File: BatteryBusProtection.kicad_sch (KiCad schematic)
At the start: 14 parts, among them Q10 SIRA99DP-T1-GE3, Q7 SIRA99DP-T1-GE3, Q8 SIRA99DP-T1-GE3, Q9 SIRA99DP-T1-GE3, U3 LTC4412xS6, U4 LTC4412xS6

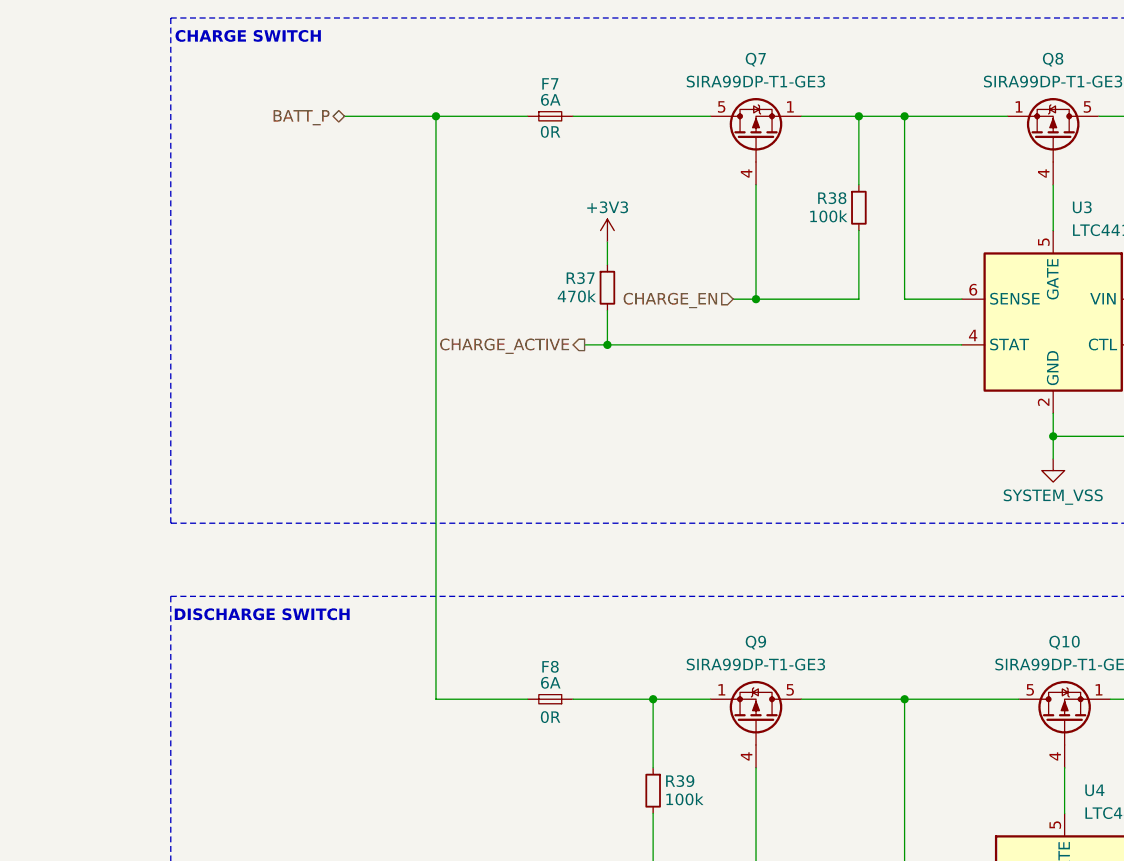
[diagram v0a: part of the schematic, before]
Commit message: Replaced old Interfaces with MCU
Added STM32U375CET6 mcu to board controlling the heaters and charging based on fuel gauge output.

Uses CAN for communication with mainboard.
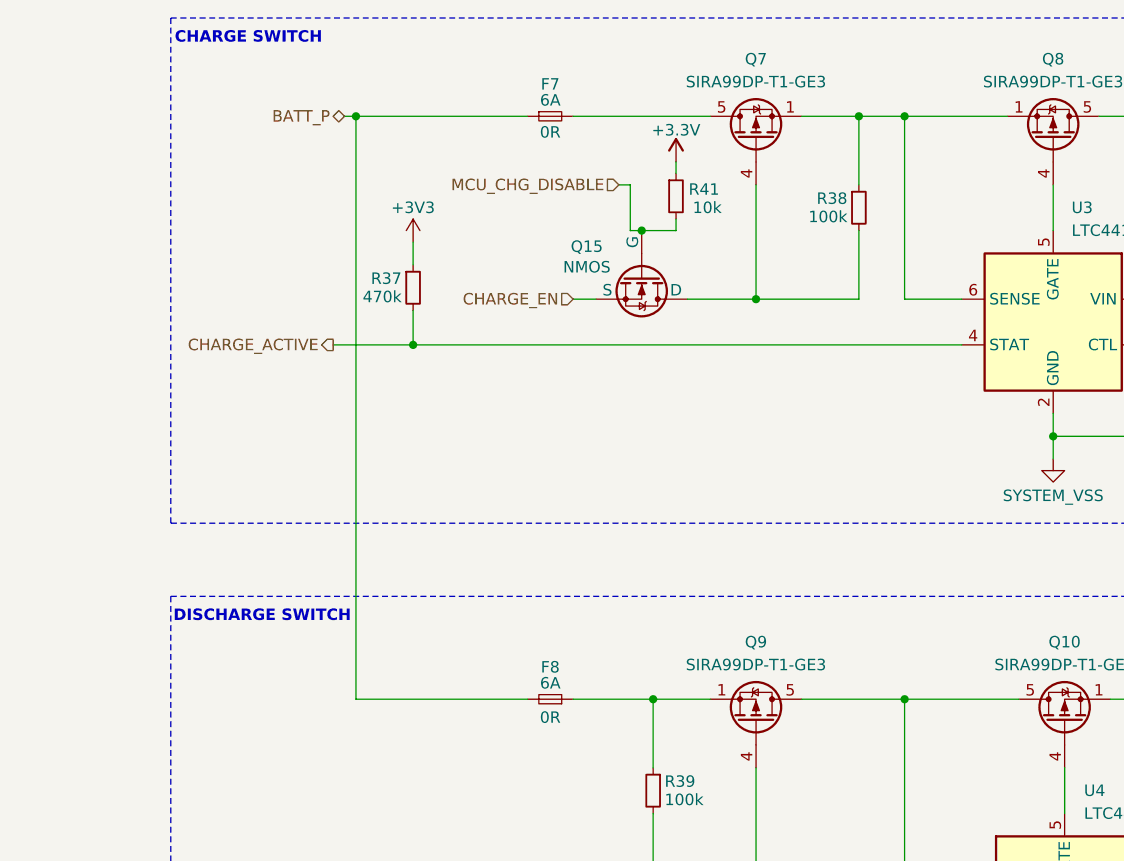
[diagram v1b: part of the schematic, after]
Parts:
- added Q15: NMOS, symbol Simulation_SPICE:NMOS
- added R41: 10k, Resistor_SMD:R_0603_1608Metric, symbol Device:R_Small
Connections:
- net CHARGE_EN: now also Q15.3 (S); no longer Q7.4 (G), R38.2
- new net: Q15.1 (D), Q7.4 (G), R38.2
- new net +3.3V: R41.1
- new net MCU_CHG_DISABLE: Q15.2 (G), R41.2
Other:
- moved on the sheet: R37

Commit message: Layout in progress
In the middle of completing layout
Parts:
- Q15: value NMOS -> IRLML2803; footprint (none) -> Package_TO_SOT_SMD:SOT-23
- renumbered R41 to R71
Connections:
- net +3V3 is gone; now on net +3.3V: R37.1, R40.1
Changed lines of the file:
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@@
 			)
 		)
-		(property "Value" "NMOS"
+		(property "Value" "IRLML2803"
 			(at 117.094 62.484 90)
 			(effects
@@
 			)
 		)
-		(property "Footprint" ""
+		(property "Footprint" "Package_TO_SOT_SMD:SOT-23"
 			(at 125.73 68.58 0)
 			(effects
@@
 			)
 		)
-		(property "Value" "+3V3"
+		(property "Value" "+3.3V"
 			(at 97.79 55.88 0)
 			(effects
@@
 		(on_board yes)
 		(dnp no)
-		(property "Reference" "R41"
+		(property "Reference" "R71"
 			(at 131.826 53.848 0)
 			(effects
@@
 			(project "Avionics-Argus3-BatteryBoard"
 				(path "/b6fd875d-6e05-4440-9a05-0f0aa046a0ef/2701f768-968e-41c8-b7b5-2417f566d99b"
-					(reference "R41")
+					(reference "R71")
 					(unit 1)
 				)
@@
 			)
 		)
-		(property "Value" "+3V3"
+		(property "Value" "+3.3V"
 			(at 191.77 120.65 0)
 			(effects
